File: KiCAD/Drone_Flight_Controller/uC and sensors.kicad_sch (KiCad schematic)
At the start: 11 parts, among them SW1 SW_Push, U401 ESP32-WROOM-32, U402 DPS368, U403 BNO055

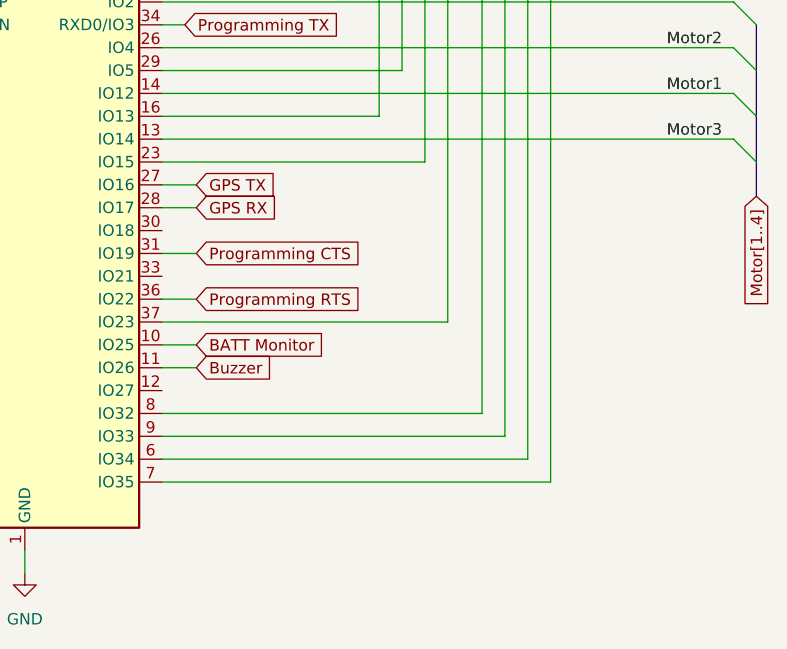
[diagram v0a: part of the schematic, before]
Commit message: Add IO connector
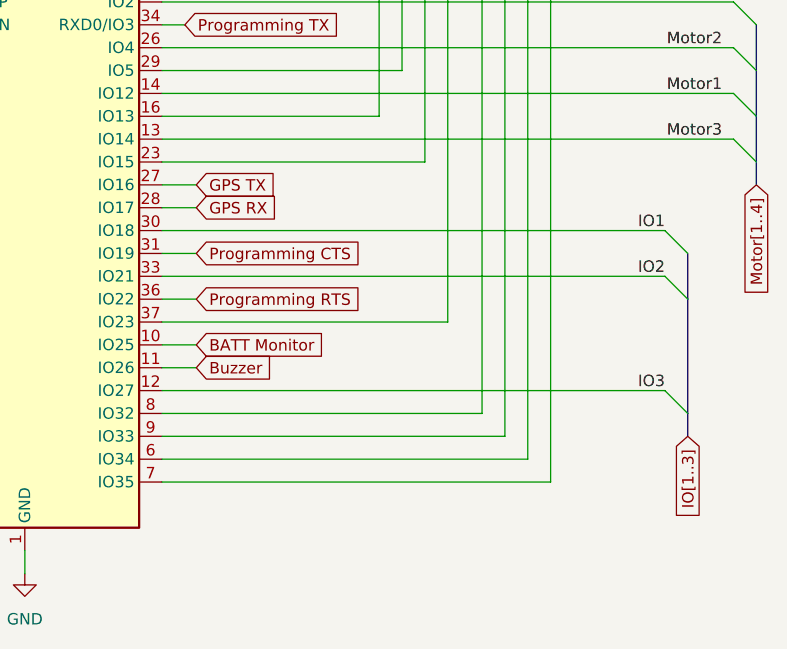
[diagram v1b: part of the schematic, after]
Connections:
- net IO3: now reaches U401.12 (IO27)
- net IO1: now reaches U401.30 (IO18)
- net IO2: now reaches U401.33 (IO21)
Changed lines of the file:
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@@
+	)
+	(bus_entry
+		(at 266.7 113.03)
+		(size 2.54 2.54)
+		(stroke
+			(width 0)
+			(type default)
+		)
 	)
 	(bus_entry
@@
 	)
 	(bus_entry
+		(at 266.7 125.73)
+		(size 2.54 2.54)
+		(stroke
+			(width 0)
+			(type default)
+		)
+	)
+	(bus_entry
+		(at 266.7 107.95)
+		(size 2.54 2.54)
+		(stroke
+			(width 0)
+			(type default)
+		)
+	)
+	(bus_entry
 		(at 274.32 97.79)
 		(size 2.54 2.54)
@@
 		)
 	)
+	(bus
+		(pts
+			(xy 269.24 115.57) (xy 269.24 110.49)
+		)
+		(stroke
+			(width 0)
+			(type default)
+		)
+	)
 	(wire
 		(pts
@@
 	(wire
 		(pts
+			(xy 210.82 113.03) (xy 266.7 113.03)
+		)
+		(stroke
+			(width 0)
+			(type default)
+		)
+	)
+	(bus
+		(pts
+			(xy 269.24 115.57) (xy 269.24 128.27)
+		)
+		(stroke
+			(width 0)
+			(type default)
+		)
+	)
+	(wire
+		(pts
 			(xy 95.25 111.76) (xy 95.25 109.22)
 		)
@@
 	(bus
 		(pts
-			(xy 276.86 104.14) (xy 276.86 100.33)
+			(xy 276.86 102.87) (xy 276.86 100.33)
 		)
 		(stroke
@@
 		)
 	)
+	(bus
+		(pts
+			(xy 269.24 130.81) (xy 269.24 128.27)
+		)
+		(stroke
+			(width 0)
+			(type default)
+		)
+	)
 	(wire
 		(pts
@@
 	(wire
 		(pts
+			(xy 210.82 107.95) (xy 266.7 107.95)
+		)
+		(stroke
+			(width 0)
+			(type default)
+		)
+	)
+	(wire
+		(pts
 			(xy 213.36 74.93) (xy 213.36 77.47)
 		)
@@
 		(pts
 			(xy 142.24 88.9) (xy 142.24 96.52)
+		)
+		(stroke
+			(width 0)
+			(type default)
+		)
+	)
+	(wire
+		(pts
+			(xy 210.82 125.73) (xy 266.7 125.73)
 		)
 		(stroke
@@
 		)
 	)
+	(label "IO3"
+		(at 266.7 125.73 180)
+		(effects
+			(font
+				(size 1.27 1.27)
+			)
+			(justify right bottom)
+		)
+	)
 	(label "Motor1"
 		(at 273.05 92.71 180)
@@
 		)
 	)
+	(label "IO2"
+		(at 266.7 113.03 180)
+		(effects
+			(font
+				(size 1.27 1.27)
+			)
+			(justify right bottom)
+		)
+	)
 	(label "Motor4"
 		(at 273.05 82.55 180)
+		(effects
+			(font
+				(size 1.27 1.27)
+			)
+			(justify right bottom)
+		)
+	)
+	(label "IO1"
+		(at 266.7 107.95 180)
 		(effects
 			(font
@@
 	(global_label "Motor[1..4]"
 		(shape input)
-		(at 276.86 104.14 270)
+		(at 276.86 102.87 270)
 		(fields_autoplaced yes)
 		(effects
@@
 		)
 		(property "Intersheetrefs" "${INTERSHEET_REFS}"
-			(at 276.86 117.7085 90)
+			(at 276.86 116.4385 90)
 			(effects
 				(font
@@
 				(hide yes)
 			)
+		)
+	)
+	(global_label "IO[1..3]"
+		(shape input)
+		(at 269.24 130.81 270)
+		(fields_autoplaced yes)
+		(effects
+			(font
+				(size 1.27 1.27)
+			)
+			(justify right)
+		)
+		(property "Intersheetrefs" "${INTERSHEET_REFS}"
+			(at 269.24 141.0525 90)
+			(effects
+				(font
+					(size 1.27 1.27)
+				)
+				(justify right)
+				(hide yes)
+			)

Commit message: Reannotate
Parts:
- renumbered C3 to C301, C401 to C302, C4 to C303, C402 to C304, R401 to R301, R1 to R302, R2 to R303, SW1 to SW301, U402 to U301, U403 to U302, U401 to U303
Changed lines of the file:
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@@
 		(on_board yes)
 		(dnp no)
-		(property "Reference" "U401"
+		(property "Reference" "U303"
 			(at 179.578 103.632 90)
 			(effects
@@
 			(project "Drone_Flight_Controller"
 				(path "/05daaa24-e506-4b9a-9564-8bf799413ca8/be1bc5c9-9814-4f01-a307-b935c6145e5a"
-					(reference "U401")
+					(reference "U303")
 					(unit 1)
 				)
@@
 		(dnp no)
 		(fields_autoplaced yes)
-		(property "Reference" "#PWR0406"
+		(property "Reference" "#PWR0307"
 			(at 95.25 118.11 0)
 			(effects
@@
 			(project "Drone_Flight_Controller"
 				(path "/05daaa24-e506-4b9a-9564-8bf799413ca8/be1bc5c9-9814-4f01-a307-b935c6145e5a"
-					(reference "#PWR0406")
+					(reference "#PWR0307")
 					(unit 1)
 				)
@@
 		(dnp no)
 		(fields_autoplaced yes)
-		(property "Reference" "#PWR0402"
+		(property "Reference" "#PWR0302"
 			(at 95.25 69.85 0)
 			(effects
@@
 			(project ""
 				(path "/05daaa24-e506-4b9a-9564-8bf799413ca8/be1bc5c9-9814-4f01-a307-b935c6145e5a"
-					(reference "#PWR0402")
+					(reference "#PWR0302")
 					(unit 1)
 				)
@@
 		(on_board yes)
 		(dnp no)
-		(property "Reference" "#PWR07"
+		(property "Reference" "#PWR0305"
 			(at 142.24 105.41 0)
 			(effects
@@
 			(project "Drone_Flight_Controller"
 				(path "/05daaa24-e506-4b9a-9564-8bf799413ca8/be1bc5c9-9814-4f01-a307-b935c6145e5a"
-					(reference "#PWR07")
+					(reference "#PWR0305")
 					(unit 1)
 				)
@@
 		(dnp no)
 		(fields_autoplaced yes)
-		(property "Reference" "#PWR0405"
+		(property "Reference" "#PWR0308"
 			(at 195.58 152.4 0)
 			(effects
@@
 			(project "Drone_Flight_Controller"
 				(path "/05daaa24-e506-4b9a-9564-8bf799413ca8/be1bc5c9-9814-4f01-a307-b935c6145e5a"
-					(reference "#PWR0405")
+					(reference "#PWR0308")
 					(unit 1)
 				)
@@
 		(dnp no)
 		(fields_autoplaced yes)
-		(property "Reference" "#PWR08"
+		(property "Reference" "#PWR0303"
 			(at 142.24 73.66 0)
 			(effects
@@
 			(project "Drone_Flight_Controller"
 				(path "/05daaa24-e506-4b9a-9564-8bf799413ca8/be1bc5c9-9814-4f01-a307-b935c6145e5a"
-					(reference "#PWR08")
+					(reference "#PWR0303")
 					(unit 1)
 				)
@@
 		(on_board yes)
 		(dnp no)
-		(property "Reference" "C3"
+		(property "Reference" "C301"
 			(at 149.86 81.28 90)
 			(effects
@@
 			(project ""
 				(path "/05daaa24-e506-4b9a-9564-8bf799413ca8/be1bc5c9-9814-4f01-a307-b935c6145e5a"
-					(reference "C3")
+					(reference "C301")
 					(unit 1)
 				)
@@
 		(on_board yes)
 		(dnp no)
-		(property "Reference" "U403"
+		(property "Reference" "U302"
 			(at 102.362 69.85 0)
 			(effects
@@
 			(project "Drone_Flight_Controller"
 				(path "/05daaa24-e506-4b9a-9564-8bf799413ca8/be1bc5c9-9814-4f01-a307-b935c6145e5a"
-					(reference "U403")
+					(reference "U302")
 					(unit 1)
 				)
@@
 		(on_board yes)
 		(dnp no)
-		(property "Reference" "SW1"
+		(property "Reference" "SW301"
 			(at 149.86 90.424 0)
 			(effects
@@
 			(project ""
 				(path "/05daaa24-e506-4b9a-9564-8bf799413ca8/be1bc5c9-9814-4f01-a307-b935c6145e5a"
-					(reference "SW1")
+					(reference "SW301")
 					(unit 1)
 				)
@@
 		(dnp no)
 		(fields_autoplaced yes)
-		(property "Reference" "C401"
+		(property "Reference" "C302"
 			(at 129.54 86.3599 0)
 			(effects
@@
 			(project "Drone_Flight_Controller"
 				(path "/05daaa24-e506-4b9a-9564-8bf799413ca8/be1bc5c9-9814-4f01-a307-b935c6145e5a"
-					(reference "C401")
+					(reference "C302")
 					(unit 1)
 				)
@@
 		(dnp no)
 		(fields_autoplaced yes)
-		(property "Reference" "R401"
+		(property "Reference" "R301"
 			(at 88.9 62.23 90)
 			(effects
@@
 			(project ""
 				(path "/05daaa24-e506-4b9a-9564-8bf799413ca8/be1bc5c9-9814-4f01-a307-b935c6145e5a"
-					(reference "R401")
+					(reference "R301")
 					(unit 1)
 				)
@@
 		(on_board yes)
 		(dnp no)
-		(property "Reference" "C4"
+		(property "Reference" "C303"
 			(at 149.86 100.076 90)
 			(effects
@@
 			(project "Drone_Flight_Controller"
 				(path "/05daaa24-e506-4b9a-9564-8bf799413ca8/be1bc5c9-9814-4f01-a307-b935c6145e5a"
-					(reference "C4")
+					(reference "C303")
 					(unit 1)
 				)
@@
 		(on_board yes)
 		(dnp no)
-		(property "Reference" "R1"
+		(property "Reference" "R302"
 			(at 209.55 71.12 90)
 			(effects
@@
 			(project "Drone_Flight_Controller"
 				(path "/05daaa24-e506-4b9a-9564-8bf799413ca8/be1bc5c9-9814-4f01-a307-b935c6145e5a"
-					(reference "R1")
+					(reference "R302")
 					(unit 1)
 				)
@@
 		(dnp no)
 		(fields_autoplaced yes)
-		(property "Reference" "#PWR0401"
+		(property "Reference" "#PWR0301"
 			(at 195.58 67.31 0)
 			(effects
@@
 			(project "Drone_Flight_Controller"
 				(path "/05daaa24-e506-4b9a-9564-8bf799413ca8/be1bc5c9-9814-4f01-a307-b935c6145e5a"
-					(reference "#PWR0401")
+					(reference "#PWR0301")
 					(unit 1)
 				)
@@
 		(on_board yes)
 		(dnp no)
-		(property "Reference" "U402"
+		(property "Reference" "U301"
 			(at 52.07 86.36 0)
 			(effects
@@
 			(project "Drone_Flight_Controller"
 				(path "/05daaa24-e506-4b9a-9564-8bf799413ca8/be1bc5c9-9814-4f01-a307-b935c6145e5a"
-					(reference "U402")
+					(reference "U301")
 					(unit 1)
 				)
@@
 		(dnp no)
 		(fields_autoplaced yes)
-		(property "Reference" "R2"
+		(property "Reference" "R303"
 			(at 149.86 66.04 90)
 			(effects
@@
 			(project ""
 				(path "/05daaa24-e506-4b9a-9564-8bf799413ca8/be1bc5c9-9814-4f01-a307-b935c6145e5a"
-					(reference "R2")
+					(reference "R303")
 					(unit 1)
 				)
@@
 		(dnp no)
 		(fields_autoplaced yes)
-		(property "Reference" "#PWR0403"
+		(property "Reference" "#PWR0304"
 			(at 45.72 87.63 0)
 			(effects
@@
 			(project "Drone_Flight_Controller"
 				(path "/05daaa24-e506-4b9a-9564-8bf799413ca8/be1bc5c9-9814-4f01-a307-b935c6145e5a"
-					(reference "#PWR0403")
+					(reference "#PWR0304")
 					(unit 1)
 				)
@@
 		(on_board yes)
 		(dnp no)
-		(property "Reference" "C402"
+		(property "Reference" "C304"
 			(at 119.38 98.298 90)
 			(effects
@@
 			(project "Drone_Flight_Controller"
 				(path "/05daaa24-e506-4b9a-9564-8bf799413ca8/be1bc5c9-9814-4f01-a307-b935c6145e5a"
-					(reference "C402")
+					(reference "C304")
 					(unit 1)
 				)
@@
 		(dnp no)
 		(fields_autoplaced yes)
-		(property "Reference" "#PWR0404"
+		(property "Reference" "#PWR0306"
 			(at 43.18 115.57 0)
 			(effects
@@
 			(project "Drone_Flight_Controller"
 				(path "/05daaa24-e506-4b9a-9564-8bf799413ca8/be1bc5c9-9814-4f01-a307-b935c6145e5a"
-					(reference "#PWR0404")
-					(unit 1)
-				)
+					(reference "#PWR0306")
+					(unit 1)
+				)

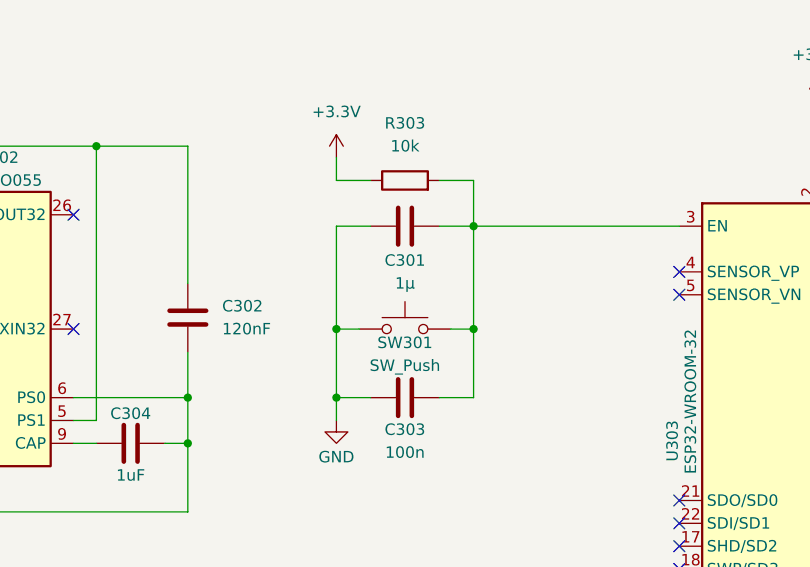
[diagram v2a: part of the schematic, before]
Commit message: Copy footprints to new parts
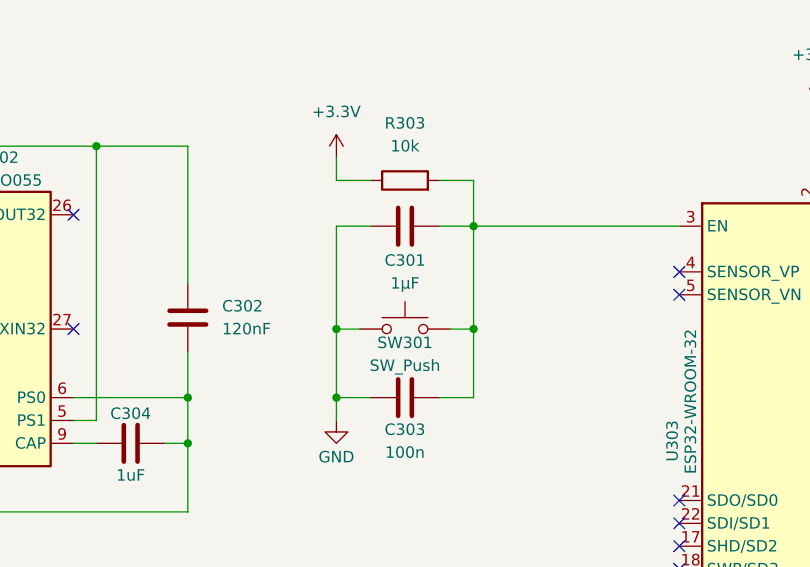
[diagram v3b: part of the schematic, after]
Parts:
- C301: value 1µ -> 1µF; footprint (none) -> Capacitor_SMD:C_0805_2012Metric_Pad1.18x1.45mm_HandSolder; Link (none) -> https://www.mouser.at/ProductDetail/Samsung-Electro-Mechani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
- R303: footprint (none) -> Resistor_SMD:R_0805_2012Metric_Pad1.20x1.40mm_HandSolder; Link (none) -> https://www.mouser.at/ProductDetail/KOA-Speer/RN73R2ATTD100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
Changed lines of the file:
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@@
 			)
 		)
-		(property "Value" "1µ"
+		(property "Value" "1µF"
 			(at 149.86 83.82 90)
 			(effects
@@
 			)
 		)
-		(property "Footprint" ""
+		(property "Footprint" "Capacitor_SMD:C_0805_2012Metric_Pad1.18x1.45mm_HandSolder"
 			(at 153.67 76.5048 0)
 			(effects
@@
 			)
 		)
-		(property "Datasheet" "~"
+		(property "Datasheet" "https://www.mouser.at/datasheet/2/585/MLCC-1837944.pdf"
 			(at 149.86 77.47 0)
 			(effects
@@
 		(property "Description" "Unpolarized capacitor"
 			(at 149.86 77.47 0)
+			(effects
+				(font
+					(size 1.27 1.27)
+				)
+				(hide yes)
+			)
+		)
+		(property "Link" "https://www.mouser.at/ProductDetail/Samsung-Electro-Mechanics/CL21B105KPFNNNE?qs=349EhDEZ59rb3V94UrmRdQ%3D%3D"
+			(at 149.86 77.47 90)
 			(effects
 				(font
@@
 			)
 		)
-		(property "Footprint" ""
+		(property "Footprint" "Resistor_SMD:R_0805_2012Metric_Pad1.20x1.40mm_HandSolder"
 			(at 149.86 74.168 90)
 			(effects
@@
 			)
 		)
-		(property "Datasheet" "~"
+		(property "Datasheet" "https://www.mouser.com/catalog/specsheets/KOA_Speer_RN73R__8_20_24.pdf"
 			(at 149.86 72.39 0)
 			(effects
@@
 			(effects
 				(font
+					(size 1.27 1.27)
+				)
+				(hide yes)
+			)
+		)
+		(property "Link" "https://www.mouser.at/ProductDetail/KOA-Speer/RN73R2ATTD1002B25?qs=sGAEpiMZZMtlubZbdhIBIMWCRdMSCzTZYWNHqlmKHZA%3D"
+			(at 149.86 72.39 90)
+			(effects
+				(font

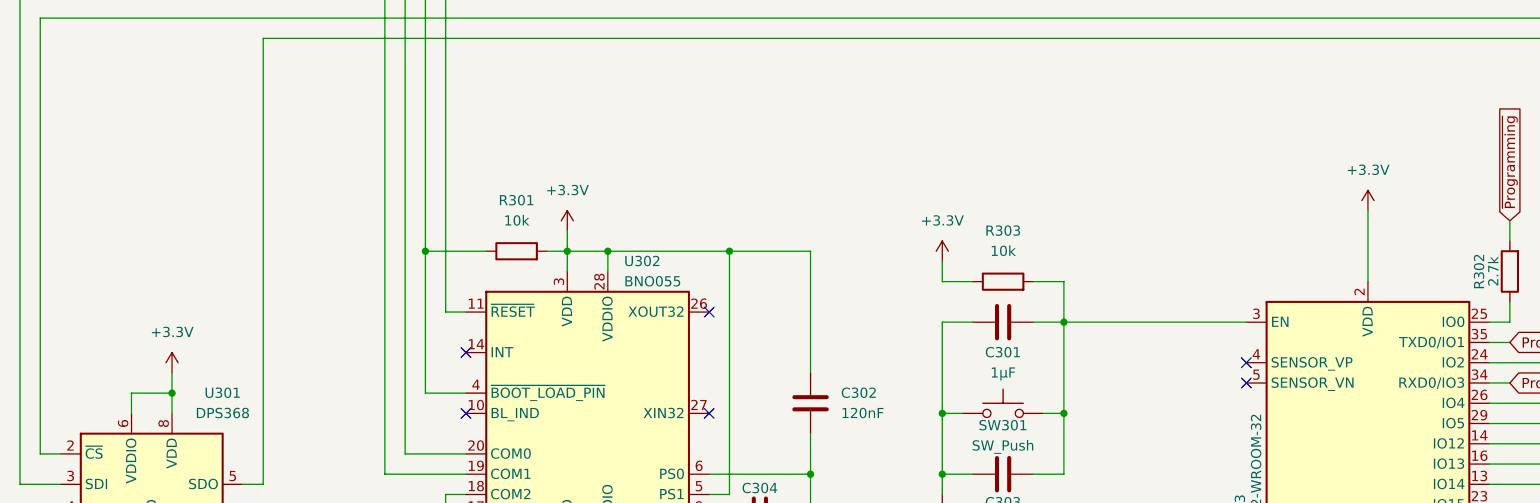
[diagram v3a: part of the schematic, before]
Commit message: Change "+3.3V" to "+3V3" for consistency
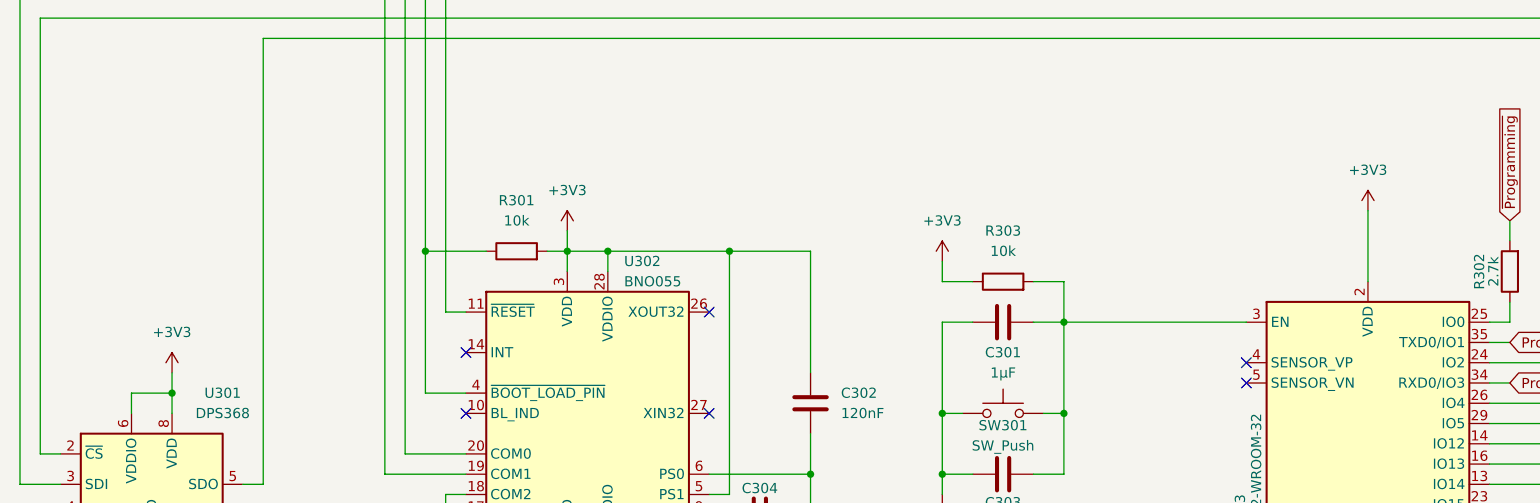
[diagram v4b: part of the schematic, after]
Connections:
- net +3.3V renamed +3V3
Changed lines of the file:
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@@
 	(title_block
 		(title "uC and sensors")
-		(date "2025-09-18")
+		(date "2025-09-19")
 		(rev "V2")
 		(company "HTL Steyr")
@@
 			)
 		)
-		(property "Value" "+3.3V"
+		(property "Value" "+3V3"
 			(at 95.25 60.96 0)
 			(effects
@@
 			)
 		)
-		(property "Value" "+3.3V"
+		(property "Value" "+3V3"
 			(at 142.24 64.77 0)
 			(effects
@@
 			)
 		)
-		(property "Value" "+3.3V"
+		(property "Value" "+3V3"
 			(at 195.58 58.42 0)
 			(effects
@@
 			)
 		)
-		(property "Value" "+3.3V"
+		(property "Value" "+3V3"
 			(at 45.72 78.74 0)
 			(effects

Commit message: Fixing errors
Fixing errors
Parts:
- SW301: footprint (none) -> Connector_PinHeader_2.54mm:PinHeader_1x02_P2.54mm_Vertical
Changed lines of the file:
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@@
 			)
 		)
-		(property "Footprint" ""
+		(property "Footprint" "Connector_PinHeader_2.54mm:PinHeader_1x02_P2.54mm_Vertical"
 			(at 149.86 83.82 0)
 			(effects

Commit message: Fix Schematic PCB parity
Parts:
- SW301: footprint Connector_PinHeader_2.54mm:PinHeader_1x02_P2.54mm_Vertical -> Button_Switch_SMD:SW_Push_1P1T_NO_CK_KSC6xxJ
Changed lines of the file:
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@@
 			)
 		)
-		(property "Footprint" "Connector_PinHeader_2.54mm:PinHeader_1x02_P2.54mm_Vertical"
+		(property "Footprint" "Button_Switch_SMD:SW_Push_1P1T_NO_CK_KSC6xxJ"
 			(at 149.86 83.82 0)
 			(effects
